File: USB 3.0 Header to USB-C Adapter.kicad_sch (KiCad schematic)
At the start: 0 parts

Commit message: Modify KiCAD Schematic
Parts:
- added U1: ~, symbol .:USB_Type_E_Female
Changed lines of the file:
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@@
 	(generator_version "9.0")
 	(paper "A4")
+	(symbol
+		(lib_id ".:USB_Type_E_Female")
+		(at 181.61 76.2 0)
+		(unit 1)
+		(exclude_from_sim no)
+		(in_bom yes)
+		(on_board yes)
+		(dnp no)
+		(fields_autoplaced yes)
+		(property "Reference" "U1"
+			(at 181.61 60.96 0)
+			(effects
+				(font
+					(size 1.27 1.27)
+				)
+			)
+		)
+		(property "Value" "~"
+			(at 181.61 63.5 0)
+			(effects
+				(font
+					(size 1.27 1.27)
+				)
+			)
+		)
+		(property "Footprint" ""
+			(at 181.61 76.2 0)
+			(effects
+				(font
+					(size 1.27 1.27)
+				)
+				(hide yes)
+			)
+		)
+		(property "Datasheet" ""
+			(at 181.61 76.2 0)
+			(effects
+				(font
+					(size 1.27 1.27)
+				)
+				(hide yes)
+			)
+		)
+		(property "Description" ""
+			(at 181.61 76.2 0)
+			(effects
+				(font
+					(size 1.27 1.27)
+				)
+				(hide yes)
+			)
+		)
+		(pin "2"
+		)
+		(pin "4"
+		)
+		(pin "1"
+		)
+		(pin "11"
+		)
+		(pin "7"
+		)
+		(pin "8"
+		)
+		(pin "10"
+		)
+		(pin "20"
+		)
+		(pin "9"
+		)
+		(pin "10"
+		)
+		(pin "19"
+		)
+		(pin "3"
+		)
+		(pin "12"
+		)
+		(pin "13"
+		)
+		(pin "6"
+		)
+		(pin "19"
+		)
+		(pin "18"
+		)
+		(pin "5"
+		)
+		(instances
+			(project ""
+				(path "/eaa233b0-72c3-4190-bb75-dd623984fe68"
+					(reference "U1")
+					(unit 1)
+				)
+			)
+		)
+	)
 	(sheet_instances
 		(path "/"

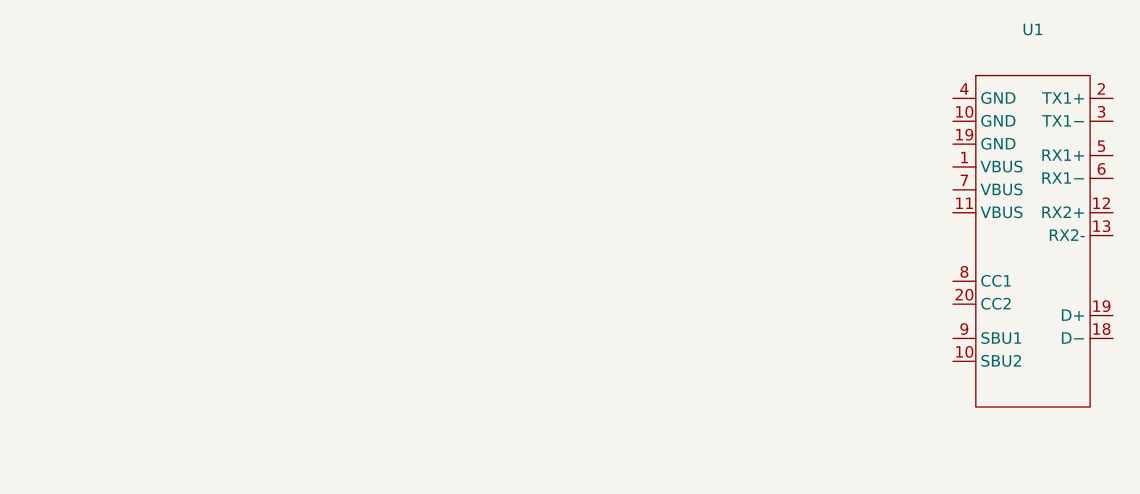
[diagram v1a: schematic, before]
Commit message: Edit KiCAD Schematic
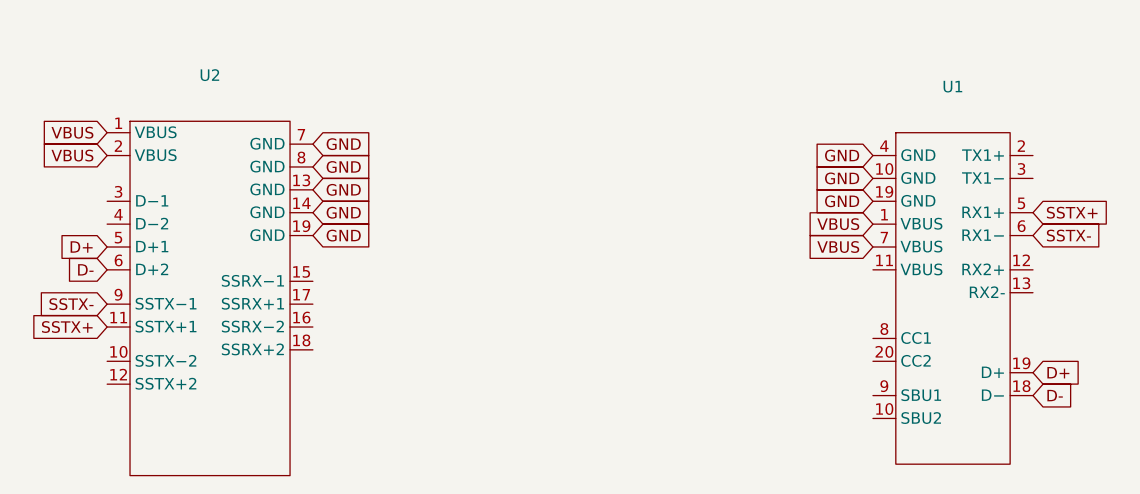
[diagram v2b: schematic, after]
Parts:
- added U2: ~, symbol .:USB3_19pin_MB_Header
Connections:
- net VBUS: now reaches U1.1 (VBUS)
- net VBUS: now also U1.7 (VBUS), U2.1 (VBUS), U2.2 (VBUS)
- net GND: now reaches U1.10 (SBU2)
- net GND: now also U1.19 (D+), U1.4 (GND), U2.13 (GND), U2.14 (GND), U2.19 (GND), U2.7 (GND), U2.8 (GND)
- net D-: now reaches U1.18 (D−)
- net D-: now also U2.6 (D+2)
- net SSTX+: now reaches U1.5 (RX1+)
- net SSTX+: now also U2.11 (SSTX+1)
- net SSTX-: now reaches U1.6 (RX1−)
- net SSTX-: now also U2.9 (SSTX−1)
- new net D+: U1.19 (D+), U2.5 (D+1)
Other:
- moved on the sheet: U1
